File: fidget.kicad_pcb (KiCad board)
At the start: 2 copper layers, 80.5 x 73.5 mm, 87 parts, among them J1 KEYSTONE 120, J2 KEYSTONE 120, U1 MCP73831-2ACI/MC, U2 ESP8285, U3 TLV70033DSE, U4 LIS2DE, U5 TPS60150, U6 TPS60150, U7 TPS60150, U8 TLV4946-2K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

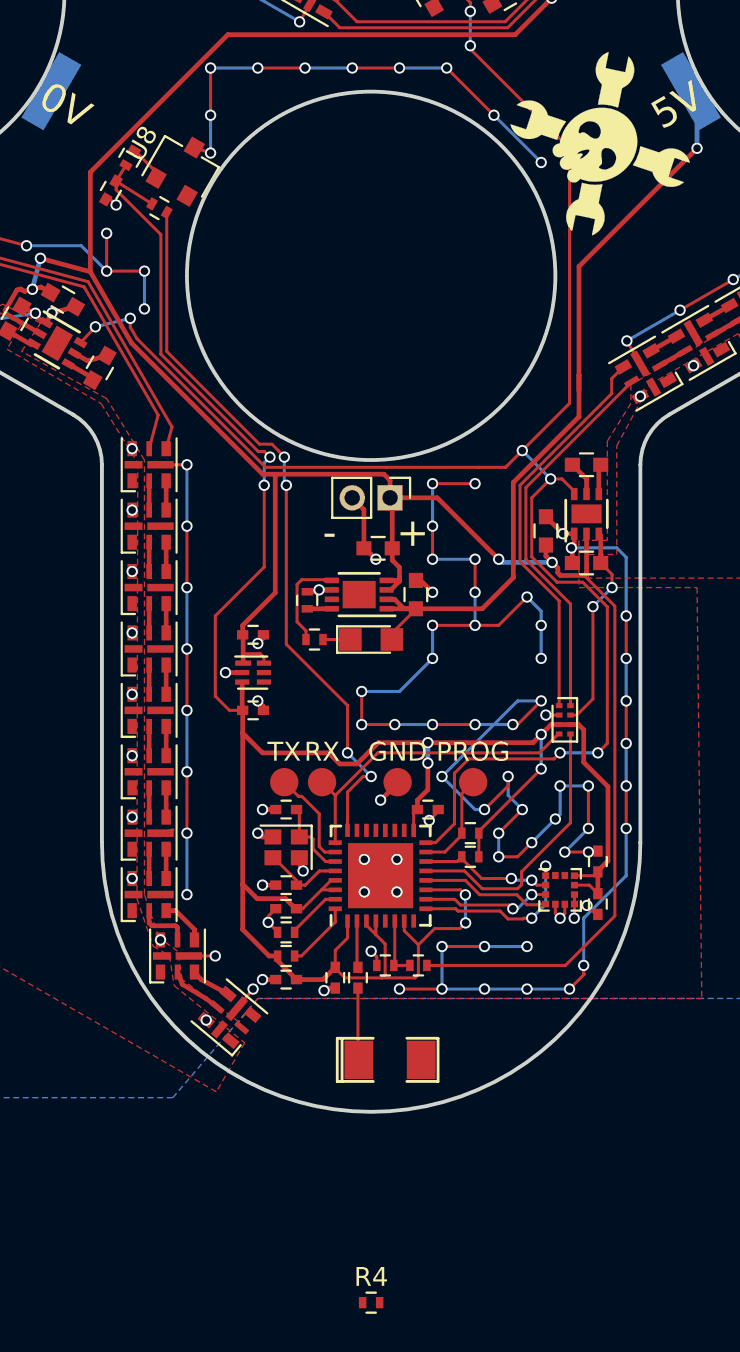
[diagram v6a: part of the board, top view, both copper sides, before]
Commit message: added SLG46140 for UVLO and power management
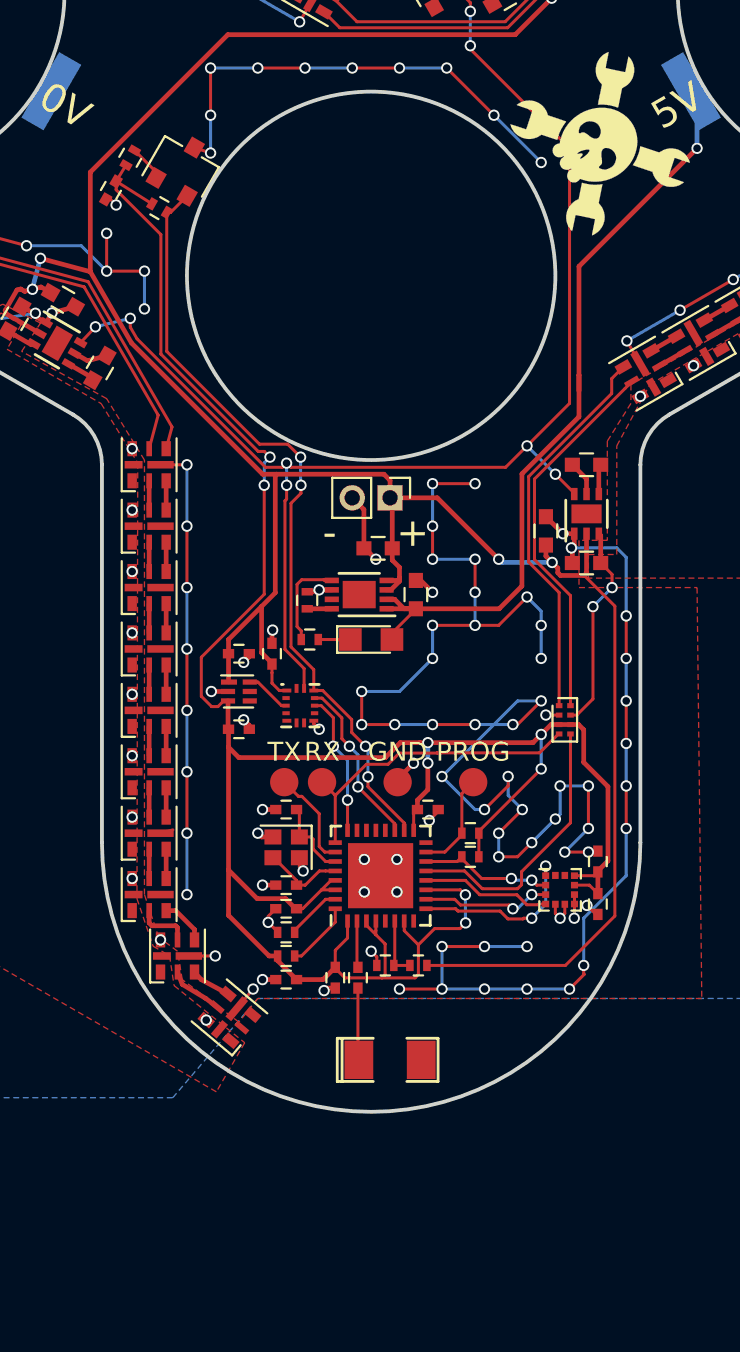
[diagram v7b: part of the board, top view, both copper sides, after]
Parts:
- removed R4: 2k, Resistors_SMD:R_0402
- added C24: 100n, Capacitors_SMD:C_0402, F.Cu at (94.8, 90.0)
- added U10: SLG46140, parts:SILEGO_STQFN-14L-1.6x2mm_Pitch0.4mm, F.Cu at (96.2, 92.8)
- R15: value 12k -> 2k
- moved C10 1.25 mm to (93.0, 90.0)
- moved C11 1.25 mm to (93.0, 94.0)
- moved U3 1.25 mm to (93.0, 92.0)
- moved R1 0.25 mm to (96.8, 89.2)
- turned R15 to 330 degrees
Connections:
- R15 pad 1: /IDX -> +3V3
- R15 pad 2: +3V3 -> /IDX
- U2 pad 16: /ENL -> (no net)
- U2 pad 18: (no net) -> /IDX
- U2 pad 19: (no net) -> /ENL1
- U2 pad 24: /IDX -> /LDO1
- U3 pad 6: +BATT -> /LDO
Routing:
- net /ENL: track 89.6 -> 71.7 mm
- net /ENL1: track 0.00 -> 8.99 mm, vias 0 -> 2
- net /LDO1: track 0.00 -> 7.53 mm, vias 0 -> 2
- net +BATT: track 136.2 -> 141.3 mm
- net /IDX: track 38.3 -> 41.0 mm
- net /LDO: track 0.00 -> 2.44 mm
- net GND: track 325.7 -> 327.0 mm, vias 180 -> 182
- net +3V3: track 129.6 -> 130.4 mm
- net +5V: track 42.1 -> 42.6 mm
